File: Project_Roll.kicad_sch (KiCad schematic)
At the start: 73 parts, among them J1 TB002-500-02BE, J10 Conn_01x04, J11 Conn_01x04, J12 Conn_01x02, J13 TB002-500-02BE, J14 TB002-500-02BE, J15 TB002-500-02BE, J16 TB002-500-02BE, J17 Conn_01x03, J2 TB002-500-02BE, J3 TB002-500-02BE, J4 TB002-500-02BE, J5 TB002-500-02BE, J6 Conn_01x05, J7 Conn_01x05, J8 Conn_01x04, J9 Conn_01x04, Q1 IRFS7430TRLPBF, U1 AP62300TWU, U2 GY-521, U3 ESP32-DEVKIT-V1, U4 MIC5504-3.3YM5

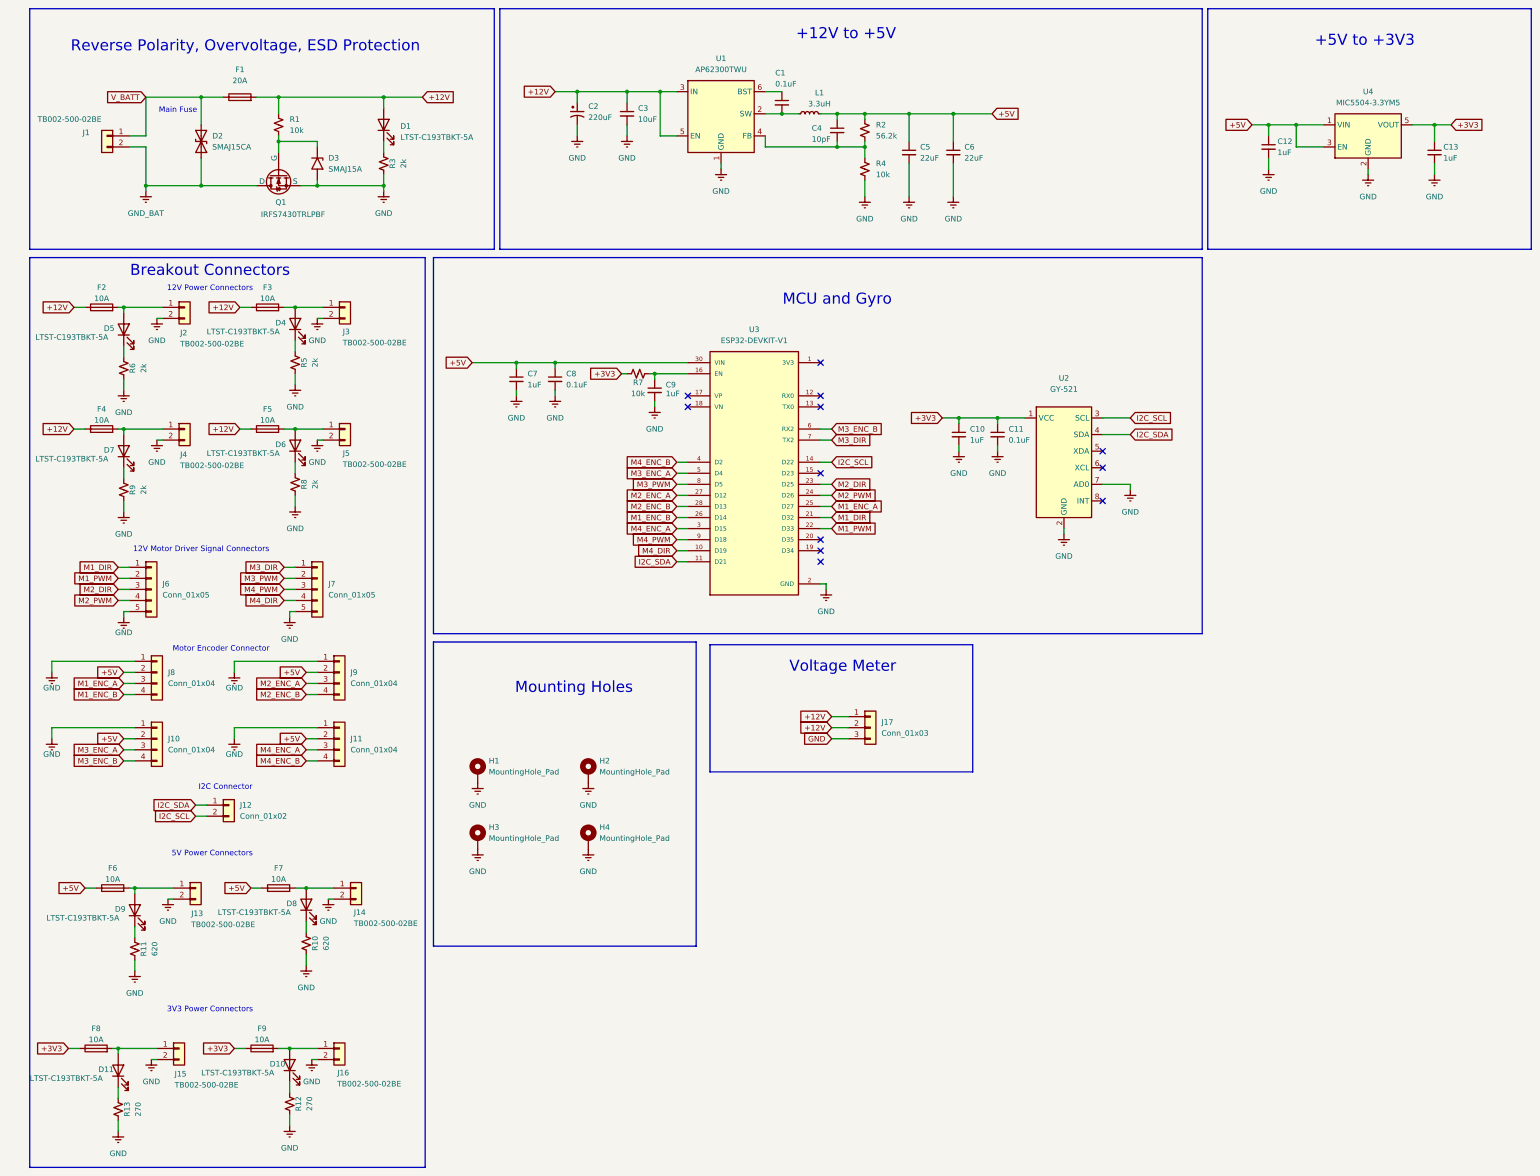
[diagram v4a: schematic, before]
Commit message: Separated schematic into sheets
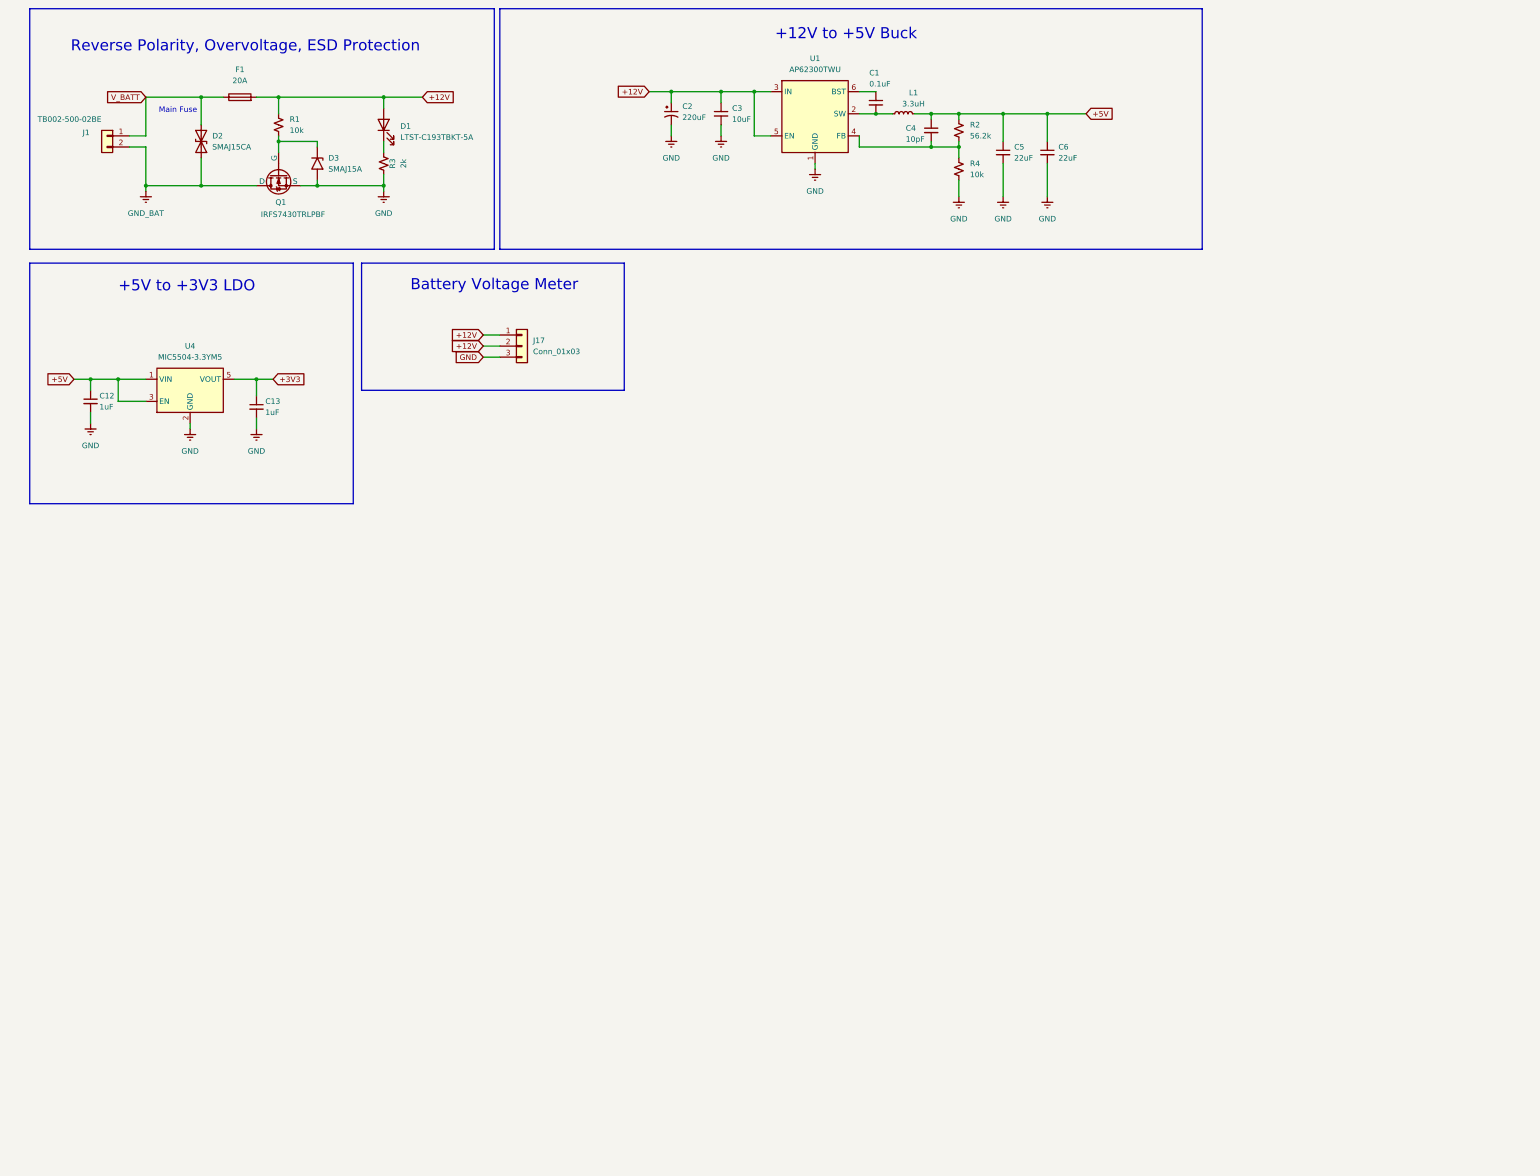
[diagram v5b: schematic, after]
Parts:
- removed C10, C7, C9: 1uF, Capacitor_SMD:C_0603_1608Metric_Pad1.08x0.95mm_HandSolder, symbol Device:C_Small
- removed C11, C8: 0.1uF, Capacitor_SMD:C_0603_1608Metric_Pad1.08x0.95mm_HandSolder, symbol Device:C_Small
- removed D10, D11, D4, D5, D6, D7, D8, D9: LTST-C193TBKT-5A, Diode_SMD:D_0603_1608Metric_Pad1.05x0.95mm_HandSolder, symbol Device:LED
- removed F2, F3, F4, F5, F6, F7, F8, F9: 10A, BB8 Footprints:CONN_3557-2_KEY, symbol Device:Fuse
- removed H1, H2, H3, H4: MountingHole_Pad, MountingHole:MountingHole_3.2mm_M3_DIN965_Pad, symbol Mechanical:MountingHole_Pad
- removed J10, J11, J8, J9: Conn_01x04, Connector_JST:JST_PH_B4B-PH-K_1x04_P2.00mm_Vertical, symbol Connector_Generic:Conn_01x04
- removed J12: Conn_01x02, Connector_JST:JST_PH_B2B-PH-K_1x02_P2.00mm_Vertical, symbol Connector_Generic:Conn_01x02
- removed J13, J14, J15, J16, J2, J3, J4, J5: TB002-500-02BE, BB8 Footprints:CUI_TB002-500-02BE, symbol Connector_Generic:Conn_01x02
- removed J6, J7: Conn_01x05, Connector_JST:JST_PH_B5B-PH-K_1x05_P2.00mm_Vertical, symbol Connector_Generic:Conn_01x05
- removed R10, R11: 620, Resistor_SMD:R_0603_1608Metric_Pad0.98x0.95mm_HandSolder, symbol Device:R_Small_US
- removed R12, R13: 270, Resistor_SMD:R_0603_1608Metric_Pad0.98x0.95mm_HandSolder, symbol Device:R_Small_US
- removed R5, R6, R8, R9: 2k, Resistor_SMD:R_0603_1608Metric_Pad0.98x0.95mm_HandSolder, symbol Device:R_Small_US
- removed R7: 10k, Resistor_SMD:R_0603_1608Metric_Pad0.98x0.95mm_HandSolder, symbol Device:R_Small_US
- removed U2: GY-521, Connector_PinHeader_2.54mm:PinHeader_1x08_P2.54mm_Vertical, symbol BB8 Symbols:GY-521
- removed U3: ESP32-DEVKIT-V1, BB8 Footprints:MODULE_ESP32_DEVKIT_V1, symbol BB8 Symbols:ESP32-DEVKIT-V1
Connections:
- no-connect marks 12 -> 0
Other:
- note added: "+12V to +5V Buck"
- note added: "+5V to +3V3 LDO"
- note added: "Battery Voltage Meter"
- note removed: "+12V to +5V"
- note removed: "+5V to +3V3"
- note removed: "12V Motor Driver Signal Connectors"
- note removed: "12V Power Connectors"
- note removed: "3V3 Power Connectors"
- note removed: "5V Power Connectors"
- note removed: "Breakout Connectors"
- note removed: "I2C Connector"
- note removed: "MCU and Gyro"
- note removed: "Motor Encoder Connector"
- note removed: "Mounting Holes"
- note removed: "Voltage Meter"
- moved on the sheet: C1, C12, C13, C2, C3, C4, C5, C6, J17, L1, R2, R4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
